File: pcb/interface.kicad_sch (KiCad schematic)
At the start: 9 parts, among them J0 UJ20-C-H-G-SMT-P16-TR

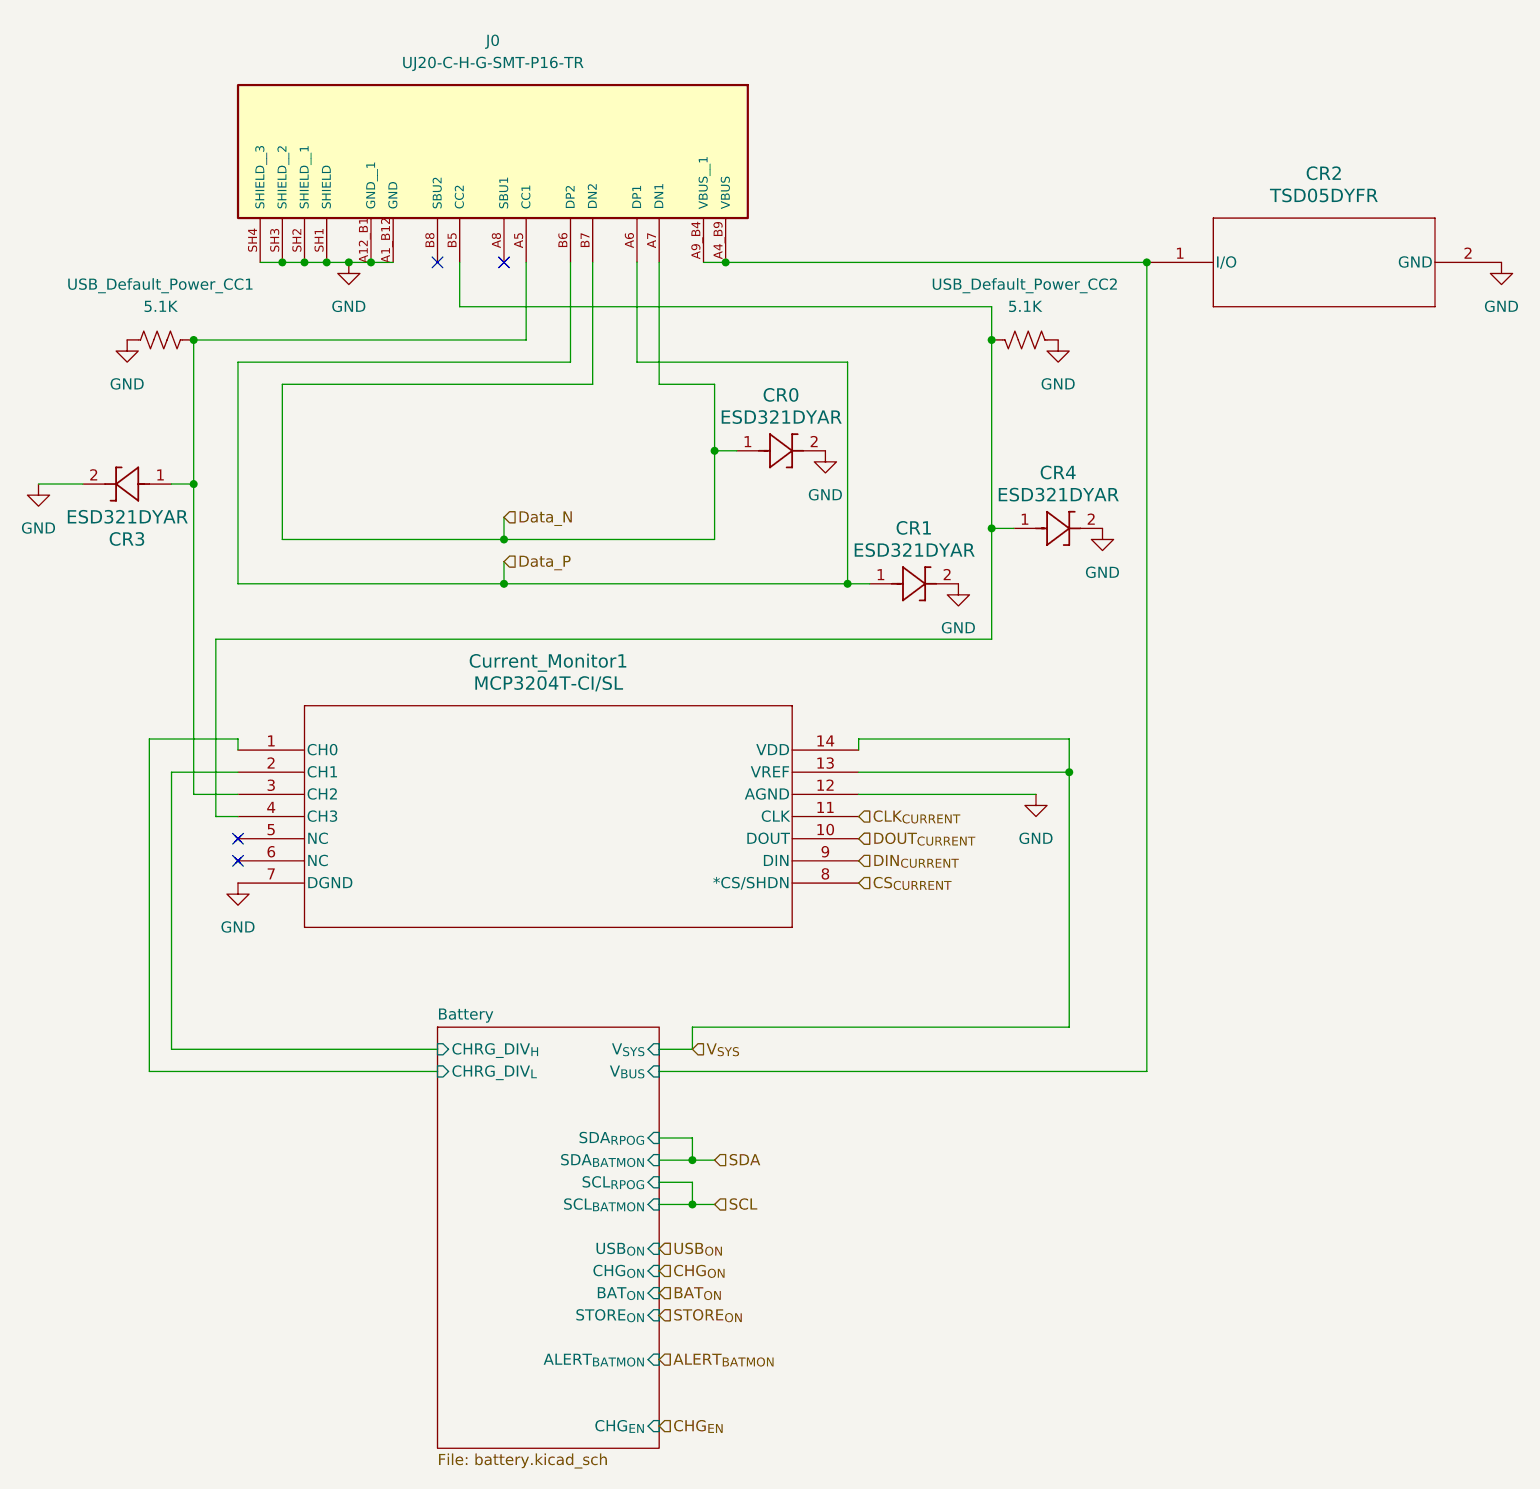
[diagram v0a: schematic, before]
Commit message: Label parts for JLCPCB
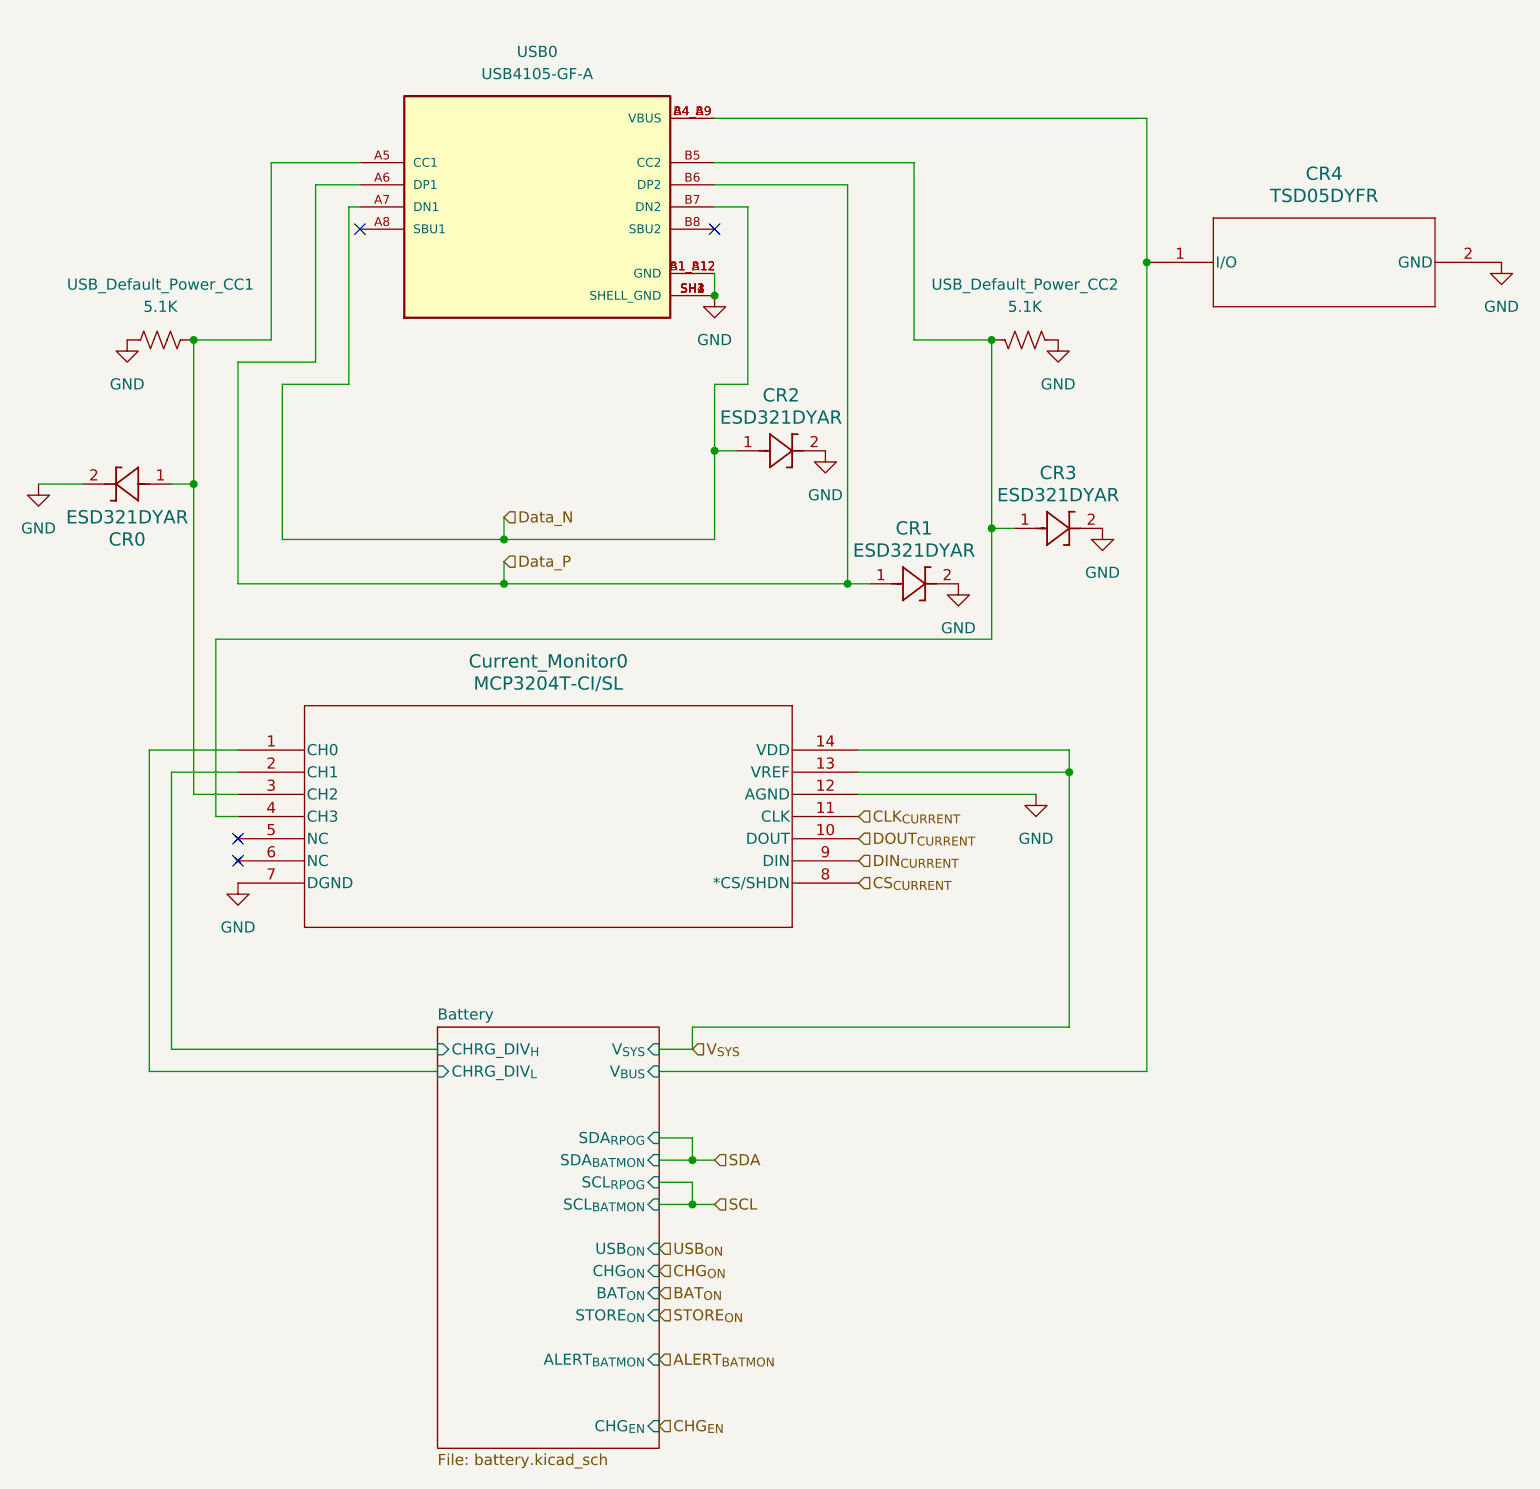
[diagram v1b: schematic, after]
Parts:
- removed J0: UJ20-C-H-G-SMT-P16-TR, UJ20-C-H-G-SMT-P16-TR:SAMESKY_UJ20-C-H-G-SMT-P16-TR, symbol UJ20-C-H-G-SMT-P16-TR:UJ20-C-H-G-SMT-P16-TR
- added USB0: USB4105-GF-A, USB4105-GF-A:GCT_USB4105-GF-A, symbol USB4105-GF-A:USB4105-GF-A
- CR0: renamed from CR3; LCSC (none) -> C20345394
- CR1: LCSC (none) -> C20345394
- CR2: renamed from CR0; LCSC (none) -> C20345394
- CR3: renamed from CR4; LCSC (none) -> C20345394
- CR4: renamed from CR2; LCSC (none) -> C22396185
- Current_Monitor0: renamed from Current_Monitor1; LCSC (none) -> C2669887
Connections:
- net Battery/V_{BUS}: now also USB0.A4_B9 (VBUS), USB0.B4_A9 (VBUS)
- net Data_N: now also USB0.A7 (DN1), USB0.B7 (DN2)
- net Data_P: now also USB0.A6 (DP1), USB0.B6 (DP2)
- net GND: now also USB0.A1_B12 (GND), USB0.B1_A12 (GND), USB0.SH1 (SHELL_GND), USB0.SH2 (SHELL_GND), USB0.SH3 (SHELL_GND), USB0.SH4 (SHELL_GND)
- net at CR0.1, Current_Monitor0.3 (CH2), USB_Default_Power_CC1.1: now also USB0.A5 (CC1)
- net at CR3.1, Current_Monitor0.4 (CH3), USB_Default_Power_CC2.1: now also USB0.B5 (CC2)

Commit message: Add DNP for right hand
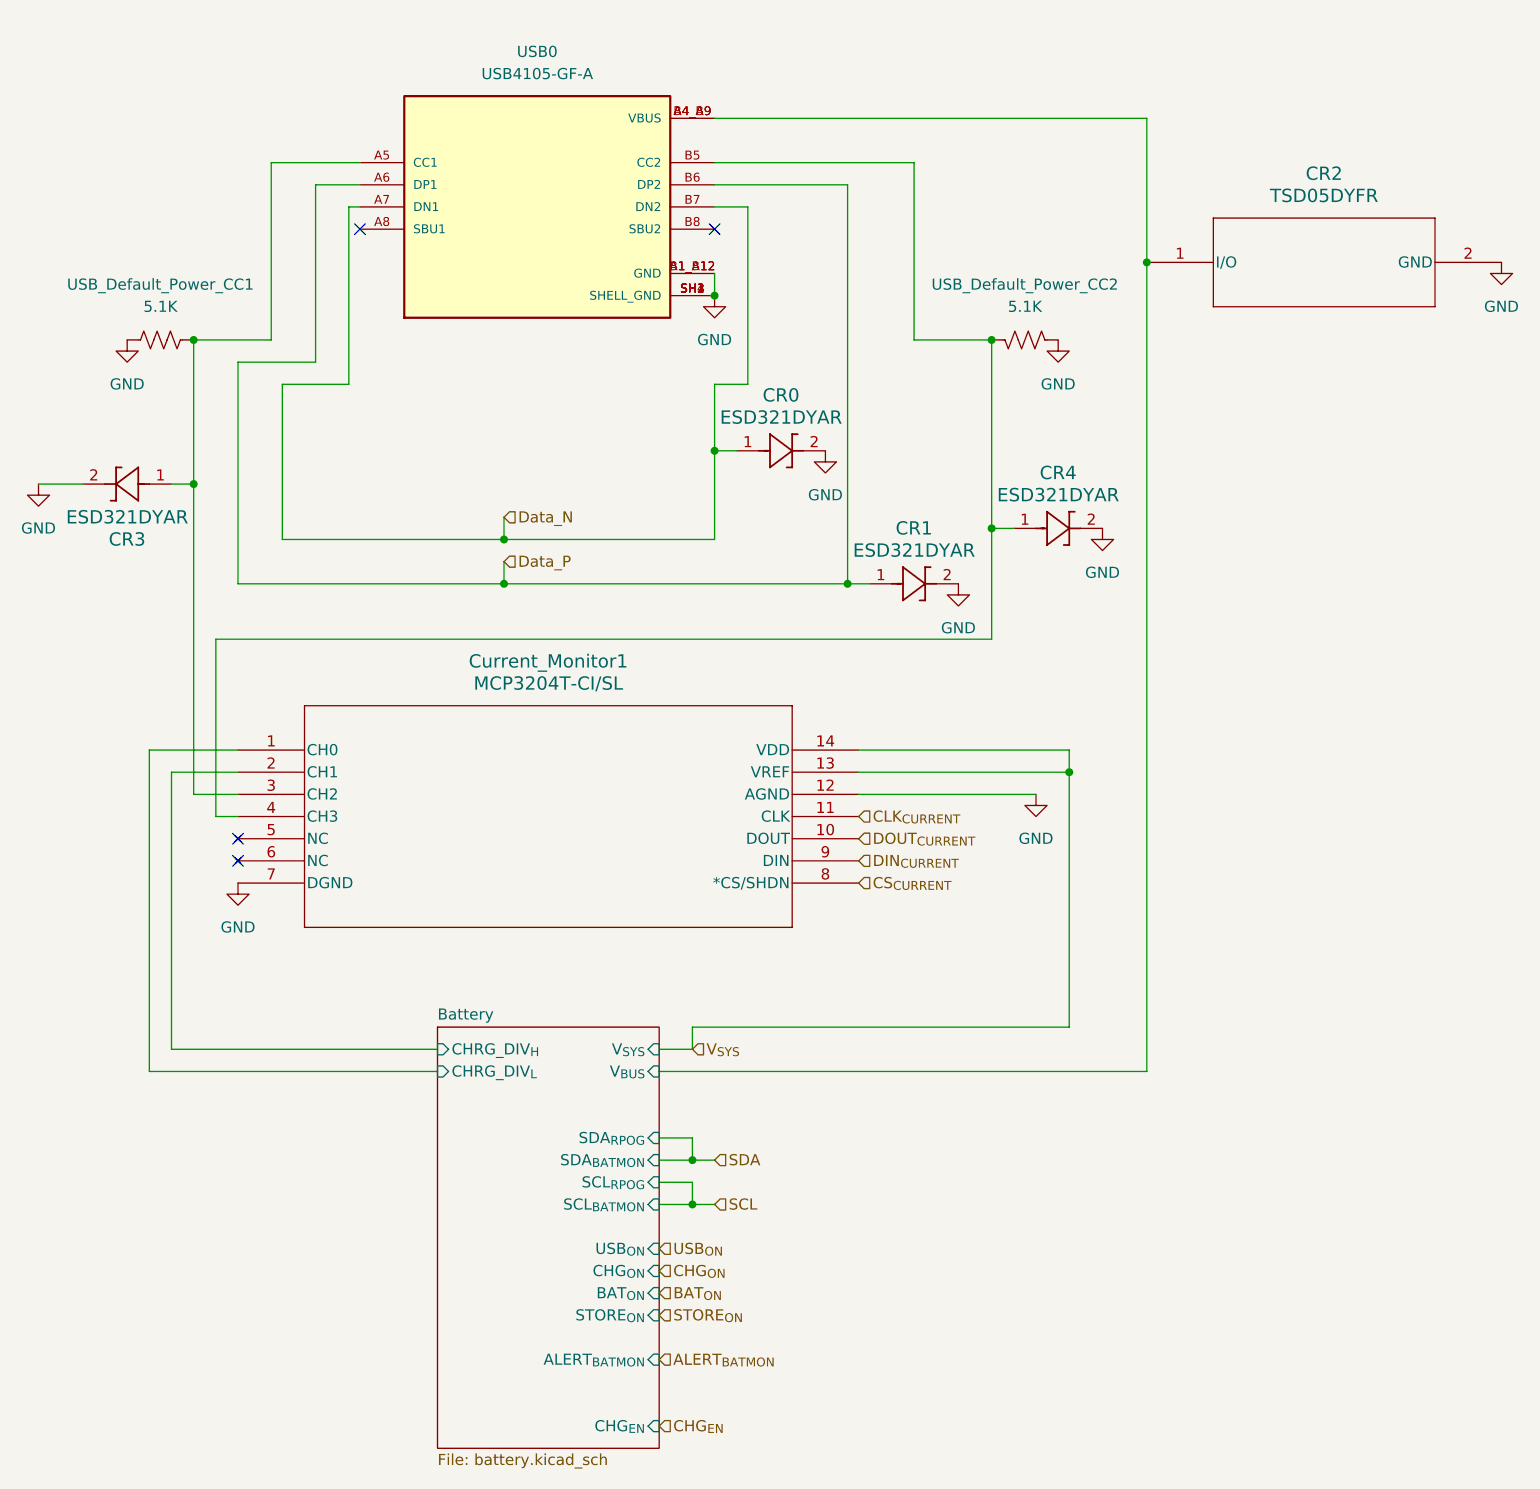
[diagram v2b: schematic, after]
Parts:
- renumbered CR2 to CR0, CR4 to CR2, CR0 to CR3, CR3 to CR4, Current_Monitor0 to Current_Monitor1
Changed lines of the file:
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@@
 		(dnp no)
 		(fields_autoplaced yes)
-		(property "Reference" "#PWR07"
+		(property "Reference" "#PWR09"
 			(at 179.07 76.2 0)
 			(effects
@@
 		(dnp no)
 		(fields_autoplaced yes)
-		(property "Reference" "#PWR037"
+		(property "Reference" "#PWR023"
 			(at 256.54 54.61 0)
 			(effects
@@
 		(dnp no)
 		(fields_autoplaced yes)
-		(property "Reference" "#PWR08"
+		(property "Reference" "#PWR021"
 			(at 194.31 91.44 0)
 			(effects
@@
 		(dnp no)
 		(fields_autoplaced yes)
-		(property "Reference" "#PWR035"
+		(property "Reference" "#PWR027"
 			(at 88.9 80.01 0)
 			(effects
@@
 		(dnp no)
 		(fields_autoplaced yes)
-		(property "Reference" "CR0"
+		(property "Reference" "CR3"
 			(at 99.06 80.01 0)
 			(effects
@@
 		(dnp no)
 		(fields_autoplaced yes)
-		(property "Reference" "USB0"
+		(property "Reference" "USB?"
 			(at 146.05 24.13 0)
 			(effects
@@
 				)
 			)
+			(project "right_hand"
+				(path "/efcccfe8-5e20-4b1b-8d3b-61fce771481e/cd3314d0-f605-42f0-be2b-644cabc7637c"
+					(reference "USB?")
+					(unit 1)
+				)
+			)
 		)
 	)
@@
 		(dnp no)
 		(fields_autoplaced yes)
-		(property "Reference" "#PWR04"
+		(property "Reference" "#PWR0105"
 			(at 111.76 125.73 0)
 			(effects
@@
 		(dnp no)
 		(fields_autoplaced yes)
-		(property "Reference" "CR4"
+		(property "Reference" "CR2"
 			(at 236.22 38.1 0)
 			(effects
@@
 		(on_board yes)
 		(dnp no)
-		(property "Reference" "Current_Monitor0"
+		(property "Reference" "Current_Monitor1"
 			(at 147.32 93.98 0)
 			(effects
@@
 		(dnp no)
 		(fields_autoplaced yes)
-		(property "Reference" "#PWR03"
+		(property "Reference" "#PWR0101"
 			(at 205.74 63.5 0)
 			(effects
@@
 		(dnp no)
 		(fields_autoplaced yes)
-		(property "Reference" "CR3"
+		(property "Reference" "CR4"
 			(at 205.74 72.39 0)
 			(effects
@@
 		(dnp no)
 		(fields_autoplaced yes)
-		(property "Reference" "#PWR016"
+		(property "Reference" "#PWR?"
 			(at 166.37 58.42 0)
 			(effects
@@
 				)
 			)
+			(project "right_hand"
+				(path "/efcccfe8-5e20-4b1b-8d3b-61fce771481e/cd3314d0-f605-42f0-be2b-644cabc7637c"
+					(reference "#PWR?")
+					(unit 1)
+				)
+			)
 		)
 	)
@@
 		(dnp no)
 		(fields_autoplaced yes)
-		(property "Reference" "#PWR05"
+		(property "Reference" "#PWR0102"
 			(at 203.2 115.57 0)
 			(effects
@@
 		(dnp no)
 		(fields_autoplaced yes)
-		(property "Reference" "#PWR02"
+		(property "Reference" "#PWR0104"
 			(at 99.06 63.5 0)
 			(effects
@@
 		(dnp no)
 		(fields_autoplaced yes)
-		(property "Reference" "CR2"
+		(property "Reference" "CR0"
 			(at 173.99 63.5 0)
 			(effects
@@
 		(dnp no)
 		(fields_autoplaced yes)
-		(property "Reference" "#PWR036"
+		(property "Reference" "#PWR028"
 			(at 210.82 85.09 0)
 			(effects
